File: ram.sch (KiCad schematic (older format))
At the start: 25 parts, among them U16 XX4256, U17 XX4256, U18 XX4256, U19 XX4256, U20 XX4256, U21 XX4256, U22 XX4256, U23 XX4256, U32 74LS139, U34 74LS373, U35 74LS244

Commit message: Add composite output
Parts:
- U16, U17, U18, U19, U20, U21, U22, U23: footprint MODULE -> Package_DIP:DIP-20_W7.62mm_Socket_LongPads
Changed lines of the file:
@@
 F 0 "U16" H 12323 7171 50  0000 L CNN
 F 1 "XX4256" H 12323 7080 50  0000 L CNN
-F 2 "MODULE" H 12095 7125 50  0001 C CNN
+F 2 "Package_DIP:DIP-20_W7.62mm_Socket_LongPads" H 12095 7125 50  0001 C CNN
 F 3 "DOCUMENTATION" H 12095 7125 50  0001 C CNN
 	2    12095 7125
@@
 F 0 "U20" H 13208 7171 50  0000 L CNN
 F 1 "XX4256" H 13208 7080 50  0000 L CNN
-F 2 "MODULE" H 12980 7125 50  0001 C CNN
+F 2 "Package_DIP:DIP-20_W7.62mm_Socket_LongPads" H 12980 7125 50  0001 C CNN
 F 3 "DOCUMENTATION" H 12980 7125 50  0001 C CNN
 	2    12980 7125
@@
 F 0 "U17" H 14738 7171 50  0000 L CNN
 F 1 "XX4256" H 14738 7080 50  0000 L CNN
-F 2 "MODULE" H 14510 7125 50  0001 C CNN
+F 2 "Package_DIP:DIP-20_W7.62mm_Socket_LongPads" H 14510 7125 50  0001 C CNN
 F 3 "DOCUMENTATION" H 14510 7125 50  0001 C CNN
 	2    14510 7125
@@
 F 0 "U21" H 15623 7171 50  0000 L CNN
 F 1 "XX4256" H 15623 7080 50  0000 L CNN
-F 2 "MODULE" H 15395 7125 50  0001 C CNN
+F 2 "Package_DIP:DIP-20_W7.62mm_Socket_LongPads" H 15395 7125 50  0001 C CNN
 F 3 "DOCUMENTATION" H 15395 7125 50  0001 C CNN
 	2    15395 7125
@@
 F 0 "U18" H 11438 8951 50  0000 L CNN
 F 1 "XX4256" H 11438 8860 50  0000 L CNN
-F 2 "MODULE" H 11210 8905 50  0001 C CNN
+F 2 "Package_DIP:DIP-20_W7.62mm_Socket_LongPads" H 11210 8905 50  0001 C CNN
 F 3 "DOCUMENTATION" H 11210 8905 50  0001 C CNN
 	2    11210 8905
@@
 F 0 "U22" H 12323 8951 50  0000 L CNN
 F 1 "XX4256" H 12323 8860 50  0000 L CNN
-F 2 "MODULE" H 12095 8905 50  0001 C CNN
+F 2 "Package_DIP:DIP-20_W7.62mm_Socket_LongPads" H 12095 8905 50  0001 C CNN
 F 3 "DOCUMENTATION" H 12095 8905 50  0001 C CNN
 	2    12095 8905
@@
 F 0 "U19" H 13853 8951 50  0000 L CNN
 F 1 "XX4256" H 13853 8860 50  0000 L CNN
-F 2 "MODULE" H 13625 8905 50  0001 C CNN
+F 2 "Package_DIP:DIP-20_W7.62mm_Socket_LongPads" H 13625 8905 50  0001 C CNN
 F 3 "DOCUMENTATION" H 13625 8905 50  0001 C CNN
 	2    13625 8905
@@
 F 0 "U23" H 14738 8951 50  0000 L CNN
 F 1 "XX4256" H 14738 8860 50  0000 L CNN
-F 2 "MODULE" H 14510 8905 50  0001 C CNN
+F 2 "Package_DIP:DIP-20_W7.62mm_Socket_LongPads" H 14510 8905 50  0001 C CNN
 F 3 "DOCUMENTATION" H 14510 8905 50  0001 C CNN
 	2    14510 8905

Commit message: Fix power-up reset
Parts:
- C16, C17, C18, C19, C20: footprint (none) -> Raemixx500:C_Axial_L6.3mm_D2.5mm_P10.16mm
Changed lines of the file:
@@
 EESchema Schematic File Version 4
 LIBS:Raemix500-cache
-EELAYER 26 0
+EELAYER 29 0
 EELAYER END
 $Descr A3 16535 11693
@@
 F 0 "C16" H 11580 7176 50  0000 L CNN
 F 1 "330n" H 11580 7085 50  0000 L CNN
-F 2 "" H 11503 6980 50  0001 C CNN
+F 2 "Raemixx500:C_Axial_L6.3mm_D2.5mm_P10.16mm" H 11503 6980 50  0001 C CNN
 F 3 "~" H 11465 7130 50  0001 C CNN
 	1    11465 7130
@@
 F 0 "C17" H 13995 7176 50  0000 L CNN
 F 1 "330n" H 13995 7085 50  0000 L CNN
-F 2 "" H 13918 6980 50  0001 C CNN
+F 2 "Raemixx500:C_Axial_L6.3mm_D2.5mm_P10.16mm" H 13918 6980 50  0001 C CNN
 F 3 "~" H 13880 7130 50  0001 C CNN
 	1    13880 7130
@@
 F 0 "C20" H 15540 8956 50  0000 L CNN
 F 1 "330n" H 15540 8865 50  0000 L CNN
-F 2 "" H 15463 8760 50  0001 C CNN
+F 2 "Raemixx500:C_Axial_L6.3mm_D2.5mm_P10.16mm" H 15463 8760 50  0001 C CNN
 F 3 "~" H 15425 8910 50  0001 C CNN
 	1    15425 8910
@@
 F 0 "C18" H 10695 8956 50  0000 L CNN
 F 1 "330n" H 10695 8865 50  0000 L CNN
-F 2 "" H 10618 8760 50  0001 C CNN
+F 2 "Raemixx500:C_Axial_L6.3mm_D2.5mm_P10.16mm" H 10618 8760 50  0001 C CNN
 F 3 "~" H 10580 8910 50  0001 C CNN
 	1    10580 8910
@@
 F 0 "C19" H 13110 8956 50  0000 L CNN
 F 1 "330n" H 13110 8865 50  0000 L CNN
-F 2 "" H 13033 8760 50  0001 C CNN
+F 2 "Raemixx500:C_Axial_L6.3mm_D2.5mm_P10.16mm" H 13033 8760 50  0001 C CNN
 F 3 "~" H 12995 8910 50  0001 C CNN
 	1    12995 8910

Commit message: Fix typo
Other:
- note added: "Note: U20-23, U32 not loaded for 512K system"
- note removed: "Note: U20-23, U23 not loaded for 512K system"
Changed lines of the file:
@@
 Sheet 3 14
 Title "Rämixx500"
-Date "2019-04-24"
+Date "2019-07-12"
 Rev "1git"
 Comp "SukkoPera"
@@
 Wire Wire Line
 	6470 8260 6935 8260
-Text Notes 15910 4895 2    50   ~ 0
-Note: U20-23, U23 not loaded for 512K system
 Text Label 6060 2680 2    50   ~ 0
 ma5
@@
 Wire Bus Line
 	7335 870  7335 4715
+Text Notes 15910 4895 2    50   ~ 0
+Note: U20-23, U32 not loaded for 512K system
 $EndSCHEMATC

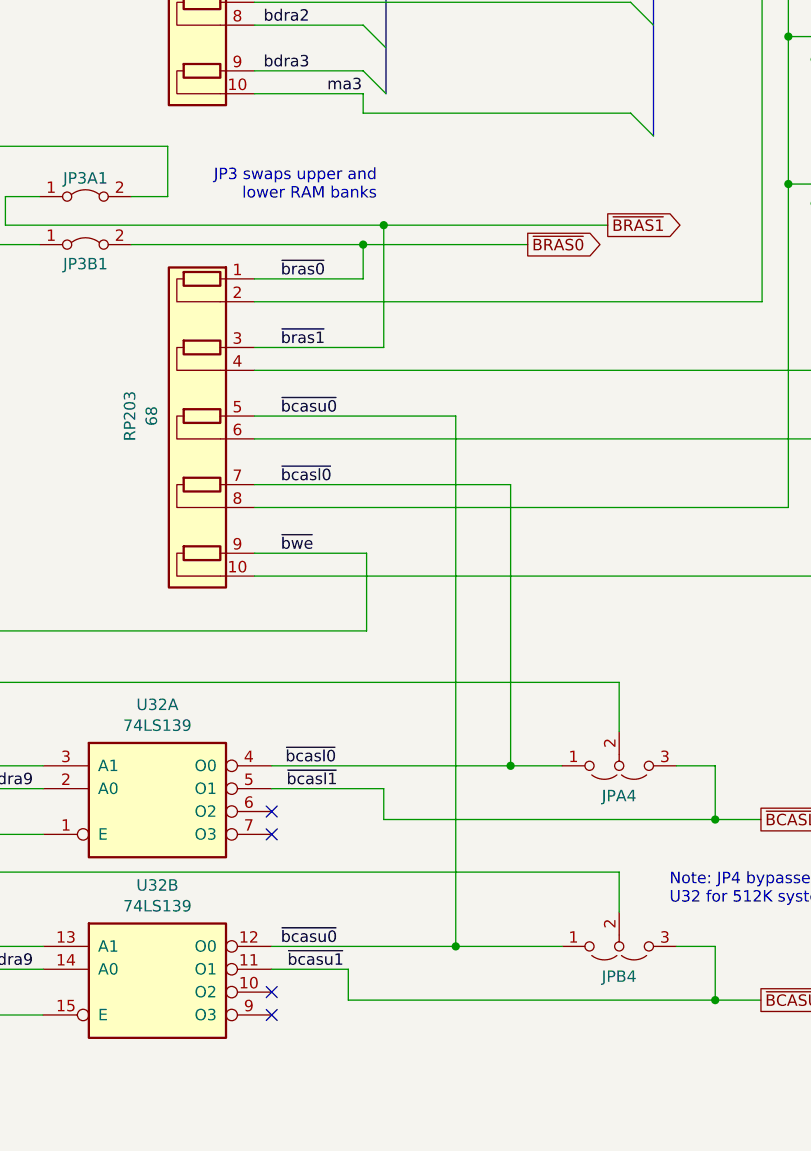
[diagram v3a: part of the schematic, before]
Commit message: Fix a lot of ERC/DRC errors
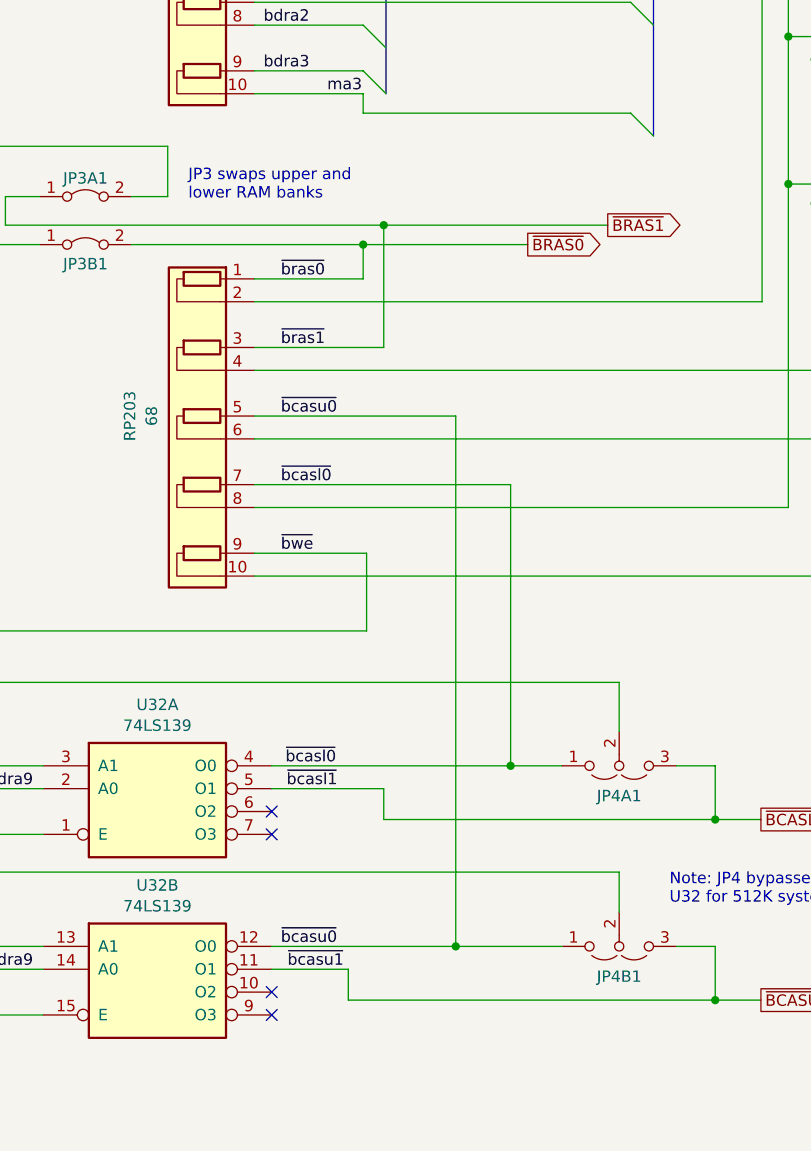
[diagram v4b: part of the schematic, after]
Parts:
- renumbered JPA4 to JP4A1, JPB4 to JP4B1
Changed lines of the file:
@@
 EESchema Schematic File Version 4
-LIBS:Raemix500-cache
-EELAYER 29 0
+EELAYER 30 0
 EELAYER END
 $Descr A3 16535 11693
@@
 Sheet 3 14
 Title "Rämixx500"
-Date "2019-07-12"
+Date "2020-04-04"
 Rev "1git"
 Comp "SukkoPera"
@@
 Wire Wire Line
 	5590 5640 6155 5640
-Text Notes 6125 5000 2    50   ~ 0
+Text Notes 5300 5000 0    50   ~ 0
 JP3 swaps upper and\nlower RAM banks
 $Comp
@@
 Connection ~ 11890 2945
 $Comp
-L Jumper:Jumper_3_Open JPA4
+L Jumper:Jumper_3_Open JP4A1
 U 1 1 5DCD8A02
 P 7185 7470
-F 0 "JPA4" H 7185 7602 50  0000 C CNN
+F 0 "JP4A1" H 7185 7602 50  0000 C CNN
 F 1 "Jumper_3_Open" H 7185 7693 50  0001 C CNN
 F 2 "Raemixx500:Jumper3-Open" H 7185 7470 50  0001 C CNN
@@
 	4210 7105 7185 7105
 $Comp
-L Jumper:Jumper_3_Open JPB4
+L Jumper:Jumper_3_Open JP4B1
 U 1 1 5E08E93D
 P 7185 8260
-F 0 "JPB4" H 7185 8392 50  0000 C CNN
+F 0 "JP4B1" H 7185 8392 50  0000 C CNN
 F 1 "Jumper_3_Open" H 7185 8483 50  0001 C CNN
 F 2 "Raemixx500:Jumper3-Open" H 7185 8260 50  0001 C CNN
@@
 Text GLabel 6785 5190 2    50   Output ~ 0
 ~BRAS0
-Wire Bus Line
-	10245 755  10245 1450
-Wire Bus Line
-	11920 755  11920 1450
-Wire Bus Line
-	13595 755  13595 1450
-Wire Bus Line
-	11920 3035 11920 3730
-Wire Bus Line
-	13595 3035 13595 3730
-Wire Bus Line
-	8430 3035 8430 3730
-Wire Bus Line
-	8430 755  8430 3035
-Wire Bus Line
-	10245 3035 10245 3730
-Wire Bus Line
-	11855 3150 11855 4230
-Wire Bus Line
-	13530 3150 13530 4230
-Wire Bus Line
-	15205 3150 15205 4230
-Wire Bus Line
-	15205 870  15205 1950
-Wire Bus Line
-	13530 870  13530 1950
-Wire Bus Line
-	11855 870  11855 1950
-Wire Bus Line
-	10180 870  10180 1950
-Wire Bus Line
-	1960 1305 1960 3625
-Wire Bus Line
-	6165 1200 6165 4530
-Wire Bus Line
-	4320 1200 4320 8260
-Wire Bus Line
-	10180 3150 10180 4230
-Wire Bus Line
-	7335 870  7335 4715
 Text Notes 15910 4895 2    50   ~ 0
 Note: U20-23, U32 not loaded for 512K system
+Wire Bus Line
+	10245 755  10245 1450
+Wire Bus Line
+	11920 755  11920 1450
+Wire Bus Line
+	13595 755  13595 1450
+Wire Bus Line
+	11920 3035 11920 3730
+Wire Bus Line
+	13595 3035 13595 3730
+Wire Bus Line
+	8430 3035 8430 3730
+Wire Bus Line
+	8430 755  8430 3035
+Wire Bus Line
+	10245 3035 10245 3730
+Wire Bus Line
+	11855 3150 11855 4230
+Wire Bus Line
+	13530 3150 13530 4230
+Wire Bus Line
+	15205 3150 15205 4230
+Wire Bus Line
+	15205 870  15205 1950
+Wire Bus Line
+	13530 870  13530 1950
+Wire Bus Line
+	11855 870  11855 1950
+Wire Bus Line
+	10180 870  10180 1950
+Wire Bus Line
+	1960 1305 1960 3625
+Wire Bus Line
+	6165 1200 6165 4530
+Wire Bus Line
+	4320 1200 4320 8260
+Wire Bus Line
+	10180 3150 10180 4230
+Wire Bus Line
+	7335 870  7335 4715
 $EndSCHEMATC
